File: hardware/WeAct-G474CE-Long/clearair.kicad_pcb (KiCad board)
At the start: 2 copper layers, 35 parts, among them J3 SPS30 wire header (1 VDD, 2 S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, J4 BME680 wire header (1 VCC, 2 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, J5 MQ131 wire header (1 VCC, 2 G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, J6 MiCS-4514 wire header (1 VCC,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, M2 80mm fan front, M3 80mm fan rear, Q1 2N7000, Q2 2N7000, Q3 2N2222A, SW1 RESET, SW2 COLD_BOOT, U5 RobotDyn AC dimmer, U6 PCF8563 RTC

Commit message: add tools for PCB placement's - AI generated scripts
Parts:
- moved R22 840.0 mm to (184.6, 123.6), turned to 90 degrees
- moved R2 838.9 mm to (160.0, 104.1), turned to 90 degrees
- moved U6 835.9 mm to (175.5, 81.0), turned to -90 degrees
- moved R14 835.2 mm to (157.5, 91.4), turned to 90 degrees
- moved R20 833.1 mm to (179.5, 123.6), turned to 90 degrees
- moved R1 833.0 mm to (154.9, 104.1), turned to 90 degrees
- moved R21 824.2 mm to (169.3, 123.6), turned to 90 degrees
- moved R15 822.9 mm to (162.6, 91.4), turned to 90 degrees
- moved R7 817.5 mm to (132.1, 104.1), turned to 90 degrees
- moved R19 817.3 mm to (164.2, 123.6), turned to 90 degrees
- moved R6 811.5 mm to (127.0, 104.1), turned to 90 degrees
- moved M3 810.6 mm to (174.4, 116.0)
- moved R9 810.6 mm to (146.8, 124.5), turned to 90 degrees
- moved R5 805.5 mm to (121.9, 104.1), turned to 90 degrees
- moved R8 805.4 mm to (137.2, 104.1), turned to 90 degrees
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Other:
- board outline added: 90.7 x 71.5 mm

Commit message: finalize wiring
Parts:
- moved U6 1.43 mm to (176.5, 80.0)
- moved M2 1.22 mm to (160.0, 116.8)
- moved M3 1.22 mm to (175.3, 116.8)
- moved R19 1.22 mm to (165.1, 124.5)
- moved R20 1.22 mm to (180.3, 124.5)
- moved R21 1.22 mm to (170.2, 124.5)
- moved R22 1.22 mm to (185.4, 124.5)
- moved BZ1 0.57 mm to (152.4, 116.8)
- moved Q3 0.57 mm to (139.7, 119.4)
- moved R9 0.57 mm to (147.3, 124.5)
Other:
- board size 90.7 x 71.5 mm -> 92.3 x 73.1 mm
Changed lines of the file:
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@@
 	(footprint "libraries:PCF8563_HW689"
 		(layer "F.Cu")
-		(at 175.5 81 -90)
+		(at 176.53 80.01 -90)
 		(descr "PCF8563 RTC module HW-689, 43 x 17 mm. 6-pin 2.54 mm header on the right short edge, pin 1 (VCC) at the top as seen in the user's photo: VCC GND SDA SCL COT INT. Two mounting holes at the left corners (position approximate from a photo). Pad positions and outline were not measured: check against the board.")
 		(tags "PCF8563 HW-689 RTC module")
@@
 	(footprint "Resistor_THT:R_Axial_DIN0207_L6.3mm_D2.5mm_P7.62mm_Horizontal"
 		(layer "F.Cu")
-		(at 164.25 123.58 90)
+		(at 165.1 124.46 90)
 		(descr "Resistor, Axial_DIN0207 series, Axial, Horizontal, pin pitch=7.62mm, 0.25W = 1/4W, length*diameter=6.3*2.5mm^2, http://cdn-reichelt.de/documents/datenblatt/B400/1_4W%23YAG.pdf")
 		(tags "Resistor Axial_DIN0207 series Axial Horizontal pin pitch 7.62mm 0.25W = 1/4W length 6.3mm diameter 2.5mm")
@@
 	(footprint "Resistor_THT:R_Axial_DIN0207_L6.3mm_D2.5mm_P7.62mm_Horizontal"
 		(layer "F.Cu")
-		(at 169.33 123.58 90)
+		(at 170.18 124.46 90)
 		(descr "Resistor, Axial_DIN0207 series, Axial, Horizontal, pin pitch=7.62mm, 0.25W = 1/4W, length*diameter=6.3*2.5mm^2, http://cdn-reichelt.de/documents/datenblatt/B400/1_4W%23YAG.pdf")
 		(tags "Resistor Axial_DIN0207 series Axial Horizontal pin pitch 7.62mm 0.25W = 1/4W length 6.3mm diameter 2.5mm")
@@
 	(footprint "Resistor_THT:R_Axial_DIN0207_L6.3mm_D2.5mm_P7.62mm_Horizontal"
 		(layer "F.Cu")
-		(at 184.57 123.58 90)
+		(at 185.42 124.46 90)
 		(descr "Resistor, Axial_DIN0207 series, Axial, Horizontal, pin pitch=7.62mm, 0.25W = 1/4W, length*diameter=6.3*2.5mm^2, http://cdn-reichelt.de/documents/datenblatt/B400/1_4W%23YAG.pdf")
 		(tags "Resistor Axial_DIN0207 series Axial Horizontal pin pitch 7.62mm 0.25W = 1/4W length 6.3mm diameter 2.5mm")
@@
 	(footprint "Connector_PinHeader_2.54mm:PinHeader_1x04_P2.54mm_Vertical"
 		(layer "F.Cu")
-		(at 174.41 115.96)
+		(at 175.26 116.84)
 		(descr "Through hole straight pin header, 1x04, 2.54mm pitch, single row")
 		(tags "Through hole pin header THT 1x04 2.54mm single row")
@@
 	(footprint "Connector_PinHeader_2.54mm:PinHeader_1x02_P2.54mm_Vertical"
 		(layer "F.Cu")
-		(at 151.83 116.84)
+		(at 152.4 116.84)
 		(descr "Through hole straight pin header, 1x02, 2.54mm pitch, single row")
 		(tags "Through hole pin header THT 1x02 2.54mm single row")
@@
 	(footprint "Resistor_THT:R_Axial_DIN0207_L6.3mm_D2.5mm_P7.62mm_Horizontal"
 		(layer "F.Cu")
-		(at 179.49 123.58 90)
+		(at 180.34 124.46 90)
 		(descr "Resistor, Axial_DIN0207 series, Axial, Horizontal, pin pitch=7.62mm, 0.25W = 1/4W, length*diameter=6.3*2.5mm^2, http://cdn-reichelt.de/documents/datenblatt/B400/1_4W%23YAG.pdf")
 		(tags "Resistor Axial_DIN0207 series Axial Horizontal pin pitch 7.62mm 0.25W = 1/4W length 6.3mm diameter 2.5mm")
@@
 	(footprint "Package_TO_SOT_THT:TO-92_Inline"
 		(layer "F.Cu")
-		(at 139.13 119.38)
+		(at 139.7 119.38)
 		(descr "TO-92 leads in-line, narrow, oval pads, drill 0.75mm (see NXP sot054_po.pdf)")
 		(tags "to-92 sc-43 sc-43a sot54 PA33 transistor")
@@
 	(footprint "Connector_PinHeader_2.54mm:PinHeader_1x04_P2.54mm_Vertical"
 		(layer "F.Cu")
-		(at 159.17 115.96)
+		(at 160.02 116.84)
 		(descr "Through hole straight pin header, 1x04, 2.54mm pitch, single row")
 		(tags "Through hole pin header THT 1x04 2.54mm single row")
@@
 	(footprint "Resistor_THT:R_Axial_DIN0207_L6.3mm_D2.5mm_P7.62mm_Horizontal"
 		(layer "F.Cu")
-		(at 146.75 124.46 90)
+		(at 147.32 124.46 90)
 		(descr "Resistor, Axial_DIN0207 series, Axial, Horizontal, pin pitch=7.62mm, 0.25W = 1/4W, length*diameter=6.3*2.5mm^2, http://cdn-reichelt.de/documents/datenblatt/B400/1_4W%23YAG.pdf")
 		(tags "Resistor Axial_DIN0207 series Axial Horizontal pin pitch 7.62mm 0.25W = 1/4W length 6.3mm diameter 2.5mm")
@@
 	)
 	(gr_rect
-		(start 97.245 56.625)
-		(end 187.96 128.095)
+		(start 97.245 55.675)
+		(end 189.505 128.815)
 		(stroke
 			(width 0.1)

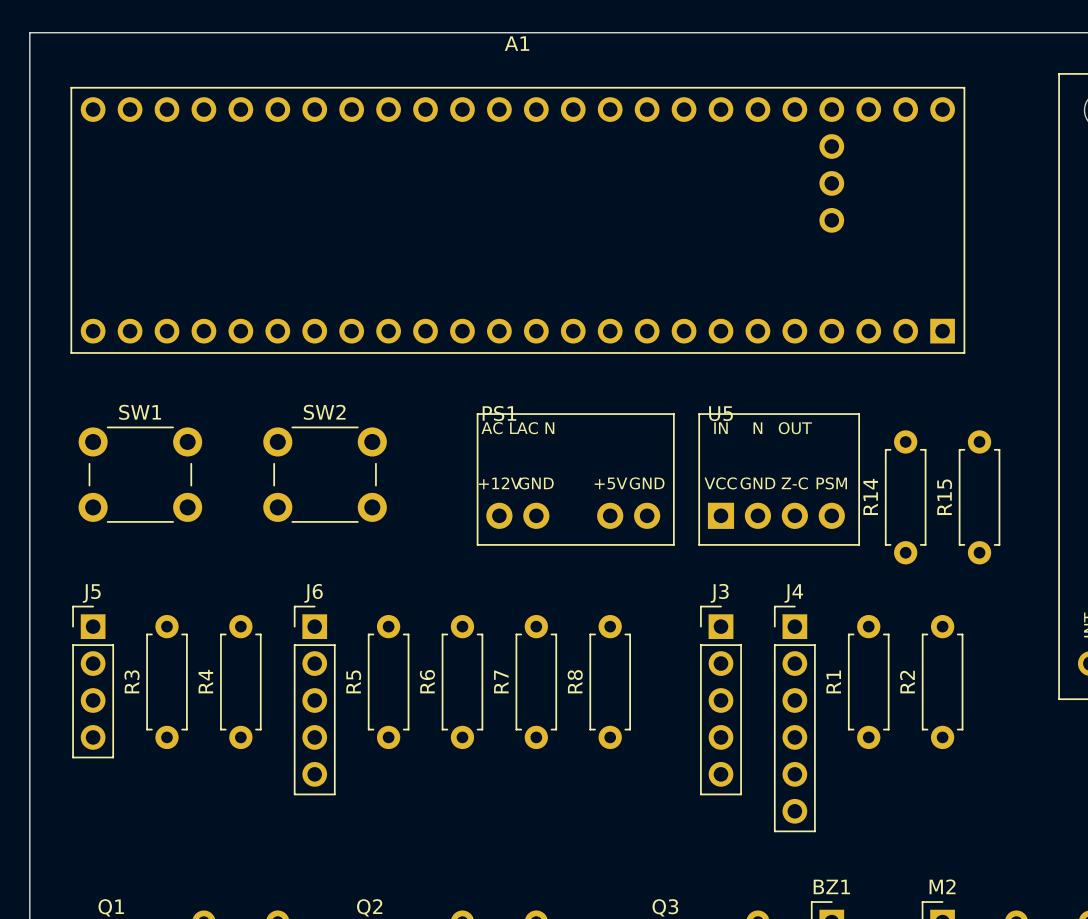
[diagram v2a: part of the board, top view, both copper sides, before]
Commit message: change the layout for helping wit the wires
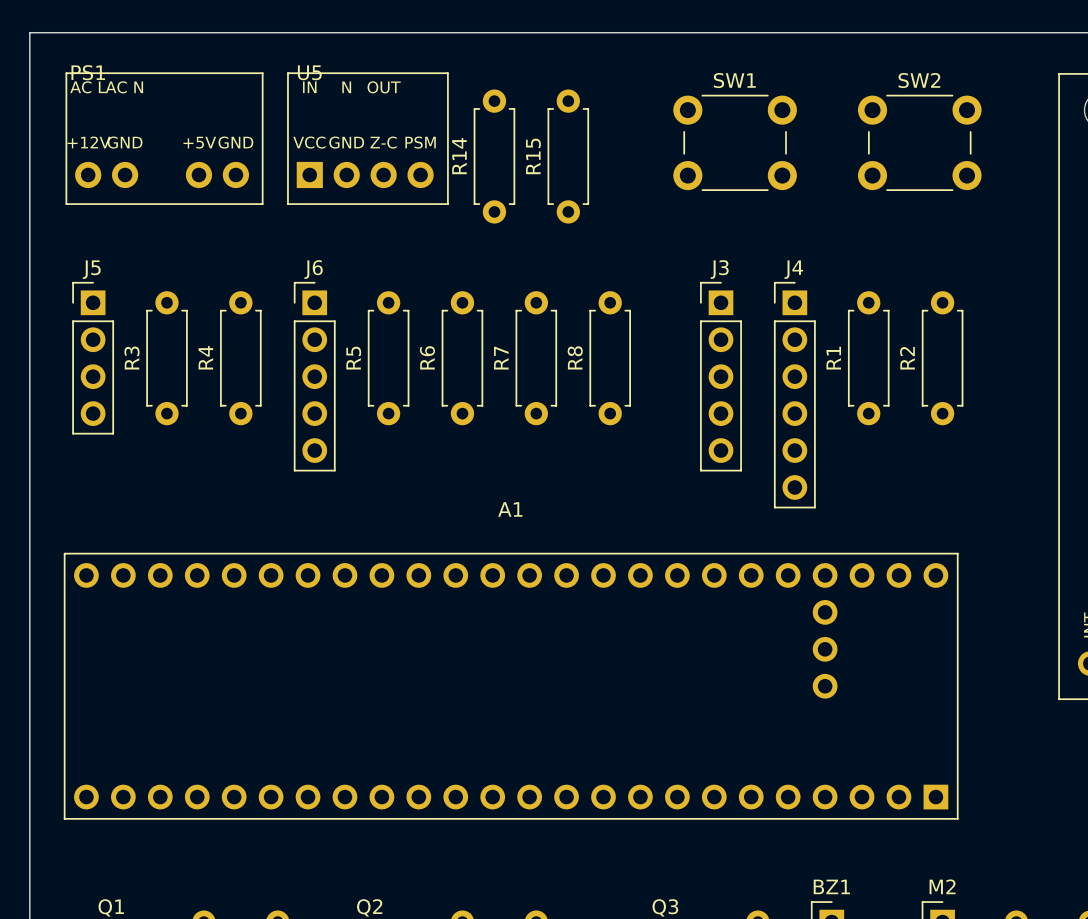
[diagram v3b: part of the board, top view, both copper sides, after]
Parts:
- moved SW1 46.8 mm to (142.5, 61.0)
- moved SW2 46.8 mm to (155.2, 61.0)
- moved U5 36.7 mm to (116.5, 65.5)
- moved PS1 36.7 mm to (101.3, 65.5)
- moved R14 36.7 mm to (129.2, 68.0)
- moved R15 36.7 mm to (134.3, 68.0)
- moved A1 32.0 mm to (130.3, 100.6)
- moved J3 22.3 mm to (144.8, 74.2)
- moved J4 22.3 mm to (149.9, 74.2)
- moved J5 22.3 mm to (101.6, 74.2)
- moved J6 22.3 mm to (116.8, 74.2)
- moved R1 22.3 mm to (154.9, 81.9)
- moved R2 22.3 mm to (160.0, 81.9)
- moved R3 22.3 mm to (106.7, 81.9)
- moved R4 22.3 mm to (111.8, 81.9)
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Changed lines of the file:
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@@
 		)
 		(property "Value" "PCF8563 RTC"
-			(at 0 10.5 90)
+			(at -23.44 10.5 90)
 			(layer "F.Fab")
 			(effects
@@
 	(footprint "Resistor_THT:R_Axial_DIN0207_L6.3mm_D2.5mm_P7.62mm_Horizontal"
 		(layer "F.Cu")
-		(at 157.48 91.44 90)
+		(at 129.2 68 90)
 		(descr "Resistor, Axial_DIN0207 series, Axial, Horizontal, pin pitch=7.62mm, 0.25W = 1/4W, length*diameter=6.3*2.5mm^2, http://cdn-reichelt.de/documents/datenblatt/B400/1_4W%23YAG.pdf")
 		(tags "Resistor Axial_DIN0207 series Axial Horizontal pin pitch 7.62mm 0.25W = 1/4W length 6.3mm diameter 2.5mm")
@@
 	(footprint "Connector_PinHeader_2.54mm:PinHeader_1x06_P2.54mm_Vertical"
 		(layer "F.Cu")
-		(at 149.86 96.52)
+		(at 149.86 74.25)
 		(descr "Through hole straight pin header, 1x06, 2.54mm pitch, single row")
 		(tags "Through hole pin header THT 1x06 2.54mm single row")
@@
 	(footprint "Resistor_THT:R_Axial_DIN0207_L6.3mm_D2.5mm_P7.62mm_Horizontal"
 		(layer "F.Cu")
-		(at 127 104.14 90)
+		(at 127 81.87 90)
 		(descr "Resistor, Axial_DIN0207 series, Axial, Horizontal, pin pitch=7.62mm, 0.25W = 1/4W, length*diameter=6.3*2.5mm^2, http://cdn-reichelt.de/documents/datenblatt/B400/1_4W%23YAG.pdf")
 		(tags "Resistor Axial_DIN0207 series Axial Horizontal pin pitch 7.62mm 0.25W = 1/4W length 6.3mm diameter 2.5mm")
@@
 	(footprint "Resistor_THT:R_Axial_DIN0207_L6.3mm_D2.5mm_P7.62mm_Horizontal"
 		(layer "F.Cu")
-		(at 162.56 91.44 90)
+		(at 134.28 68 90)
 		(descr "Resistor, Axial_DIN0207 series, Axial, Horizontal, pin pitch=7.62mm, 0.25W = 1/4W, length*diameter=6.3*2.5mm^2, http://cdn-reichelt.de/documents/datenblatt/B400/1_4W%23YAG.pdf")
 		(tags "Resistor Axial_DIN0207 series Axial Horizontal pin pitch 7.62mm 0.25W = 1/4W length 6.3mm diameter 2.5mm")
@@
 	(footprint "libraries:PSU_DC_12V_5V_Inputs"
 		(layer "F.Cu")
-		(at 129.54 88.9)
+		(at 101.26 65.46)
 		(descr "DC outputs of two separate AC-DC supplies (12 V 2 A and 5 V 2 A), each a 2-pin 2.54 mm male header soldered in two holes with AWG24 wires. Pads: 3 +12V, 5 GND (twice, one per supply), 4 +5V. Pads 1 and 2 (AC L and N) are on F.Fab only: the mains side stays off the board. Pad order and header positions are not measured: check against the supplies.")
 		(tags "PSU_DC_12V_5V_Inputs")
@@
 	(footprint "Button_Switch_THT:SW_PUSH_6mm"
 		(layer "F.Cu")
-		(at 101.6 83.82)
+		(at 142.5 61)
 		(descr "Generic 6mm SW tactile push button")
 		(tags "tact sw push 6mm")
@@
 	(footprint "Resistor_THT:R_Axial_DIN0207_L6.3mm_D2.5mm_P7.62mm_Horizontal"
 		(layer "F.Cu")
-		(at 160.02 104.14 90)
+		(at 160.02 81.87 90)
 		(descr "Resistor, Axial_DIN0207 series, Axial, Horizontal, pin pitch=7.62mm, 0.25W = 1/4W, length*diameter=6.3*2.5mm^2, http://cdn-reichelt.de/documents/datenblatt/B400/1_4W%23YAG.pdf")
 		(tags "Resistor Axial_DIN0207 series Axial Horizontal pin pitch 7.62mm 0.25W = 1/4W length 6.3mm diameter 2.5mm")
@@
 	(footprint "Button_Switch_THT:SW_PUSH_6mm"
 		(layer "F.Cu")
-		(at 114.3 83.82)
+		(at 155.2 61)
 		(descr "Generic 6mm SW tactile push button")
 		(tags "tact sw push 6mm")
@@
 	(footprint "Connector_PinHeader_2.54mm:PinHeader_1x05_P2.54mm_Vertical"
 		(layer "F.Cu")
-		(at 144.78 96.52)
+		(at 144.78 74.25)
 		(descr "Through hole straight pin header, 1x05, 2.54mm pitch, single row")
 		(tags "Through hole pin header THT 1x05 2.54mm single row")
@@
 	(footprint "Resistor_THT:R_Axial_DIN0207_L6.3mm_D2.5mm_P7.62mm_Horizontal"
 		(layer "F.Cu")
-		(at 154.94 104.14 90)
+		(at 154.94 81.87 90)
 		(descr "Resistor, Axial_DIN0207 series, Axial, Horizontal, pin pitch=7.62mm, 0.25W = 1/4W, length*diameter=6.3*2.5mm^2, http://cdn-reichelt.de/documents/datenblatt/B400/1_4W%23YAG.pdf")
 		(tags "Resistor Axial_DIN0207 series Axial Horizontal pin pitch 7.62mm 0.25W = 1/4W length 6.3mm diameter 2.5mm")
@@
 	(footprint "Resistor_THT:R_Axial_DIN0207_L6.3mm_D2.5mm_P7.62mm_Horizontal"
 		(layer "F.Cu")
-		(at 106.68 104.14 90)
+		(at 106.68 81.87 90)
 		(descr "Resistor, Axial_DIN0207 series, Axial, Horizontal, pin pitch=7.62mm, 0.25W = 1/4W, length*diameter=6.3*2.5mm^2, http://cdn-reichelt.de/documents/datenblatt/B400/1_4W%23YAG.pdf")
 		(tags "Resistor Axial_DIN0207 series Axial Horizontal pin pitch 7.62mm 0.25W = 1/4W length 6.3mm diameter 2.5mm")
@@
 	(footprint "Resistor_THT:R_Axial_DIN0207_L6.3mm_D2.5mm_P7.62mm_Horizontal"
 		(layer "F.Cu")
-		(at 132.08 104.14 90)
+		(at 132.08 81.87 90)
 		(descr "Resistor, Axial_DIN0207 series, Axial, Horizontal, pin pitch=7.62mm, 0.25W = 1/4W, length*diameter=6.3*2.5mm^2, http://cdn-reichelt.de/documents/datenblatt/B400/1_4W%23YAG.pdf")
 		(tags "Resistor Axial_DIN0207 series Axial Horizontal pin pitch 7.62mm 0.25W = 1/4W length 6.3mm diameter 2.5mm")
@@
 	(footprint "libraries:RobotDyn_Dimmer_Logic"
 		(layer "F.Cu")
-		(at 144.78 88.9)
+		(at 116.5 65.46)
 		(descr "RobotDyn AC dimmer 8A (BTA16-600B), logic side only: 4-pin 2.54 mm header VCC GND Z-C PSM, pads 1-4. Pads 5-7 (IN N OUT, the AC screw terminal) are on F.Fab only: the mains side stays off the board.")
 		(tags "RobotDyn_Dimmer_Logic")
@@
 	(footprint "Connector_PinHeader_2.54mm:PinHeader_1x05_P2.54mm_Vertical"
 		(layer "F.Cu")
-		(at 116.84 96.52)
+		(at 116.84 74.25)
 		(descr "Through hole straight pin header, 1x05, 2.54mm pitch, single row")
 		(tags "Through hole pin header THT 1x05 2.54mm single row")
@@
 	(footprint "Connector_PinHeader_2.54mm:PinHeader_1x04_P2.54mm_Vertical"
 		(layer "F.Cu")
-		(at 101.6 96.52)
+		(at 101.6 74.25)
 		(descr "Through hole straight pin header, 1x04, 2.54mm pitch, single row")
 		(tags "Through hole pin header THT 1x04 2.54mm single row")
@@
 	(footprint "Resistor_THT:R_Axial_DIN0207_L6.3mm_D2.5mm_P7.62mm_Horizontal"
 		(layer "F.Cu")
-		(at 111.76 104.14 90)
+		(at 111.76 81.87 90)
 		(descr "Resistor, Axial_DIN0207 series, Axial, Horizontal, pin pitch=7.62mm, 0.25W = 1/4W, length*diameter=6.3*2.5mm^2, http://cdn-reichelt.de/documents/datenblatt/B400/1_4W%23YAG.pdf")
 		(tags "Resistor Axial_DIN0207 series Axial Horizontal pin pitch 7.62mm 0.25W = 1/4W length 6.3mm diameter 2.5mm")
@@
 	(footprint "libraries:WeAct_STM32G474CoreBoard_Long"
 		(layer "F.Cu")
-		(at 130.81 68.58)
+		(at 130.35 100.62)
 		(descr "WeAct Studio STM32G474CEU6 Core Board (Long). Board outline (61.42x18.24mm) and 15.24mm row spacing measured from WeAct's official dimension drawing (WeAct-STM32G474CoreBoard_Long_V10 Board Shape.pdf); P5 SWD column position is approximate.")
 		(tags "STM32G474 WeAct CoreBoard Long")
@@
 	(footprint "Resistor_THT:R_Axial_DIN0207_L6.3mm_D2.5mm_P7.62mm_Horizontal"
 		(layer "F.Cu")
-		(at 121.92 104.14 90)
+		(at 121.92 81.87 90)
 		(descr "Resistor, Axial_DIN0207 series, Axial, Horizontal, pin pitch=7.62mm, 0.25W = 1/4W, length*diameter=6.3*2.5mm^2, http://cdn-reichelt.de/documents/datenblatt/B400/1_4W%23YAG.pdf")
 		(tags "Resistor Axial_DIN0207 series Axial Horizontal pin pitch 7.62mm 0.25W = 1/4W length 6.3mm diameter 2.5mm")
@@
 	(footprint "Resistor_THT:R_Axial_DIN0207_L6.3mm_D2.5mm_P7.62mm_Horizontal"
 		(layer "F.Cu")
-		(at 137.16 104.14 90)
+		(at 137.16 81.87 90)
 		(descr "Resistor, Axial_DIN0207 series, Axial, Horizontal, pin pitch=7.62mm, 0.25W = 1/4W, length*diameter=6.3*2.5mm^2, http://cdn-reichelt.de/documents/datenblatt/B400/1_4W%23YAG.pdf")
 		(tags "Resistor Axial_DIN0207 series Axial Horizontal pin pitch 7.62mm 0.25W = 1/4W length 6.3mm diameter 2.5mm")

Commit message: change the layout for helping with the wires
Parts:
- Q1, Q2, Q3: footprint Package_TO_SOT_THT:TO-92_Inline -> Package_TO_SOT_THT:TO-92_Inline_Wide

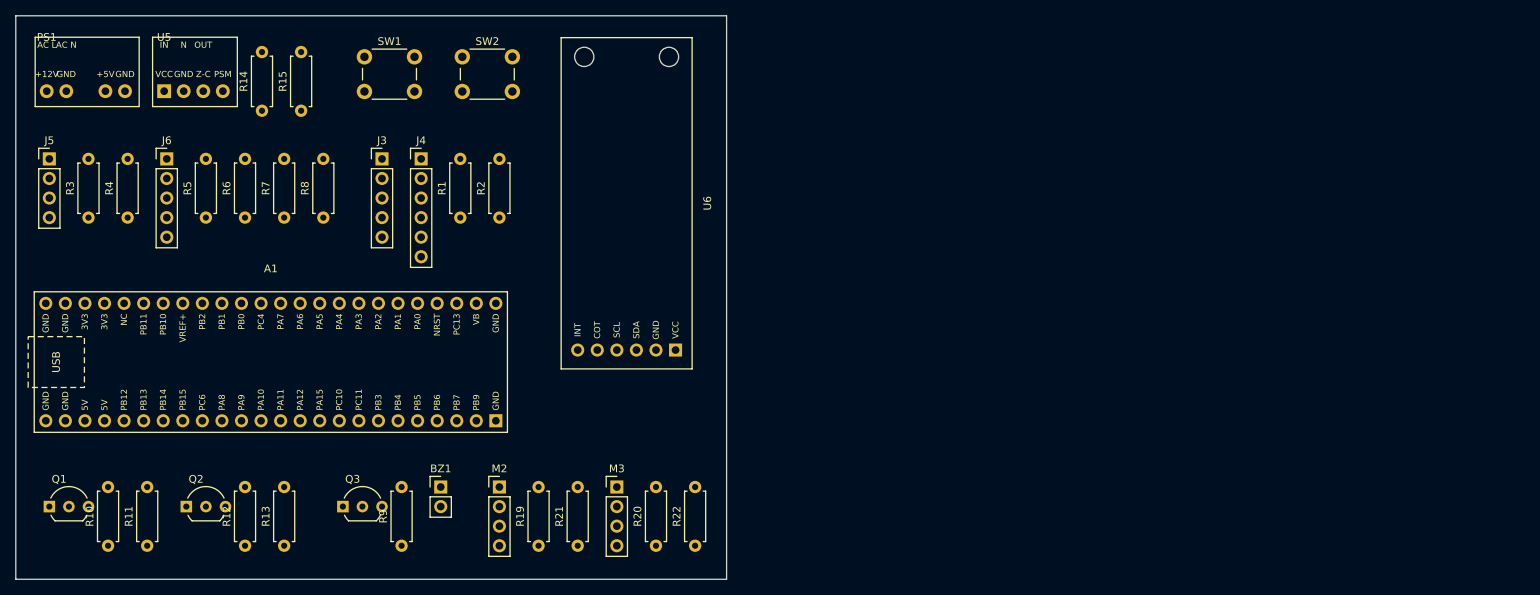
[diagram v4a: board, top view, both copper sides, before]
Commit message: split to 2 boards
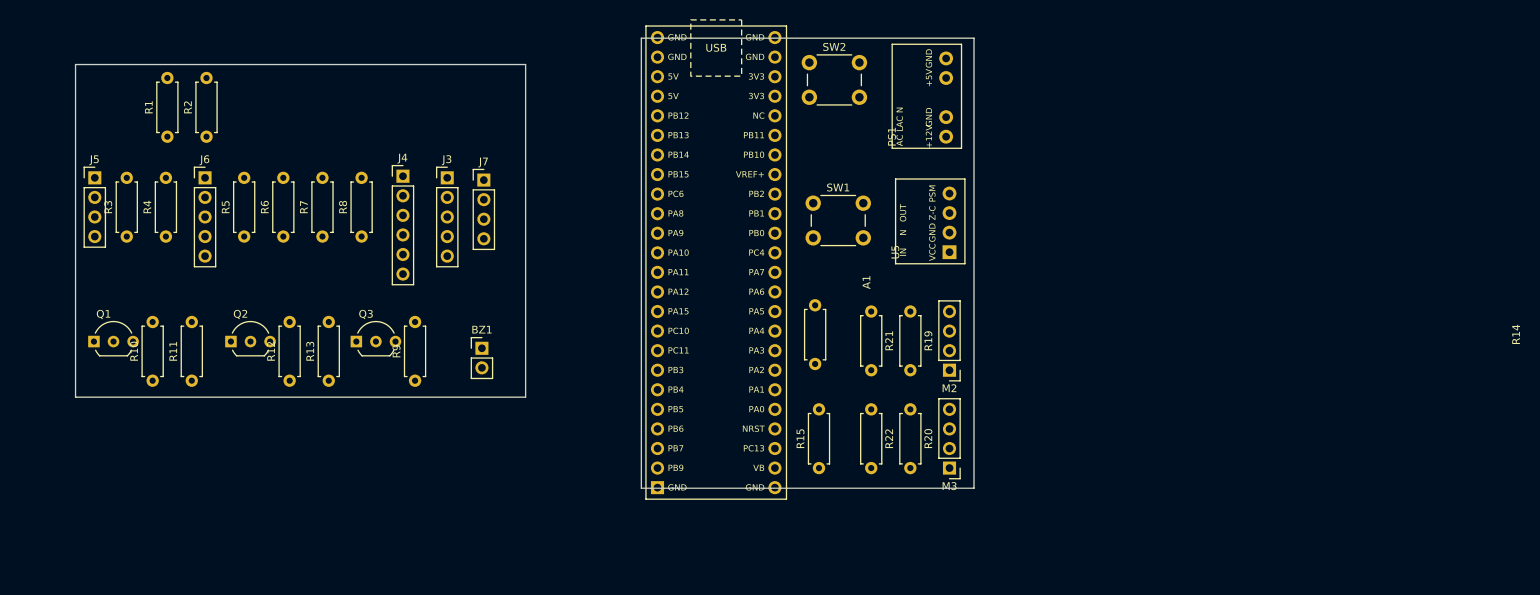
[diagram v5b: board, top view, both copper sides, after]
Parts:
- removed U6: PCF8563 RTC, libraries:PCF8563_HW689
- added J7: RTC PCF8563, Connector_PinHeader_2.54mm:PinHeader_1x04_P2.54mm_Vertical, F.Cu at (158.0, 77.0)
- moved PS1 116.9 mm to (218.0, 71.4), turned to 90 degrees
- moved U5 104.1 mm to (218.4, 86.4), turned to 90 degrees
- moved R15 81.7 mm to (201.5, 114.4)
- moved R14 79.0 mm to (201.0, 100.9)
- moved SW1 61.3 mm to (200.8, 80.0)
- moved M2 60.4 mm to (218.4, 101.7), turned to 180 degrees
- moved A1 59.2 mm to (188.2, 87.7), turned to -90 degrees
- moved R19 57.0 mm to (213.4, 94.1), turned to -90 degrees
- moved R21 48.7 mm to (208.3, 94.1), turned to -90 degrees
- moved SW2 45.1 mm to (200.2, 61.8)
- moved M3 43.3 mm to (218.4, 114.4), turned to 180 degrees
- moved R2 39.4 mm to (122.0, 71.4)
- moved R1 39.4 mm to (116.9, 71.4)
- moved R20 37.5 mm to (213.4, 106.8), turned to -90 degrees
- moved R22 28.9 mm to (208.3, 106.8), turned to -90 degrees
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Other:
- board size 92.3 x 73.1 mm -> 116.6 x 58.4 mm
